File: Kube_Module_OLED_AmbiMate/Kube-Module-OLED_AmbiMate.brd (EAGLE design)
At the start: 42.8 x 54.6 mm, 9 parts

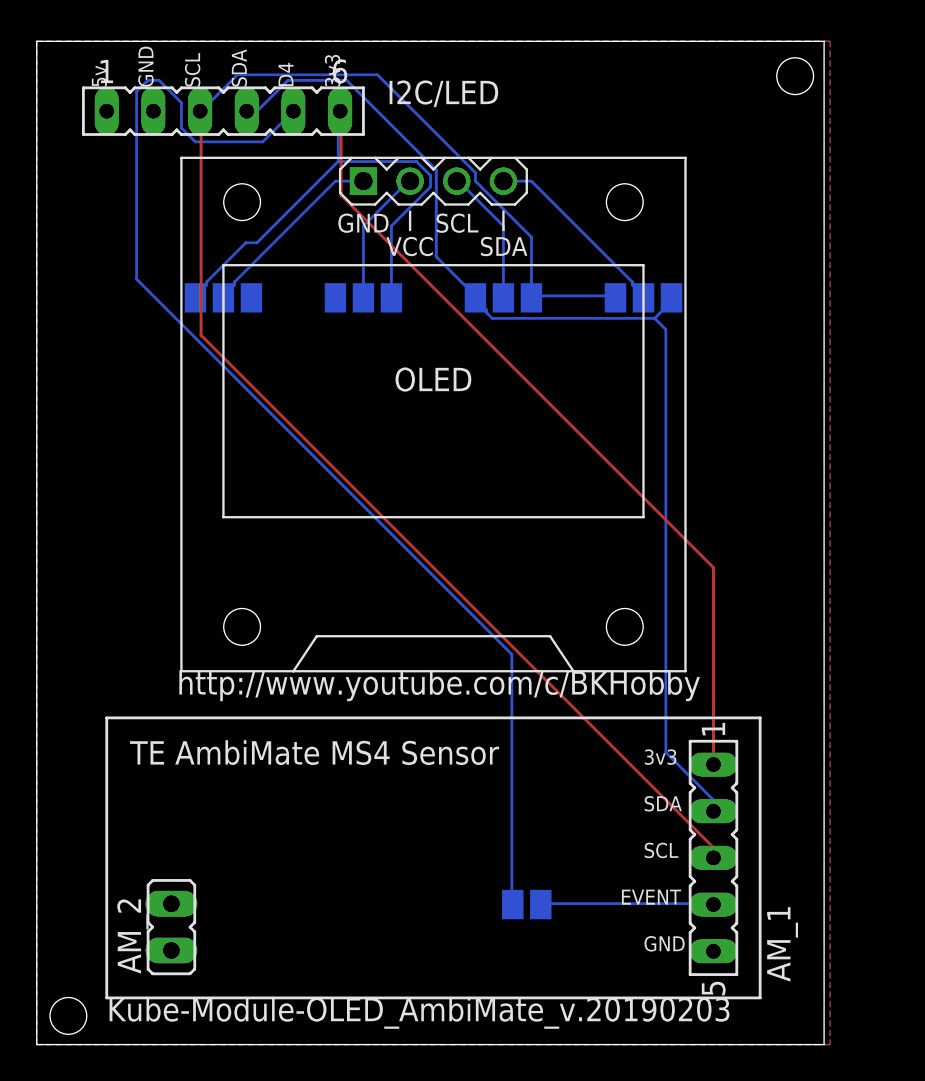
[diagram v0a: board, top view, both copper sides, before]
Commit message: Mods to OLED board to get rid of EVENT_OUT (causes boot issues since D4 needs to be held HI)
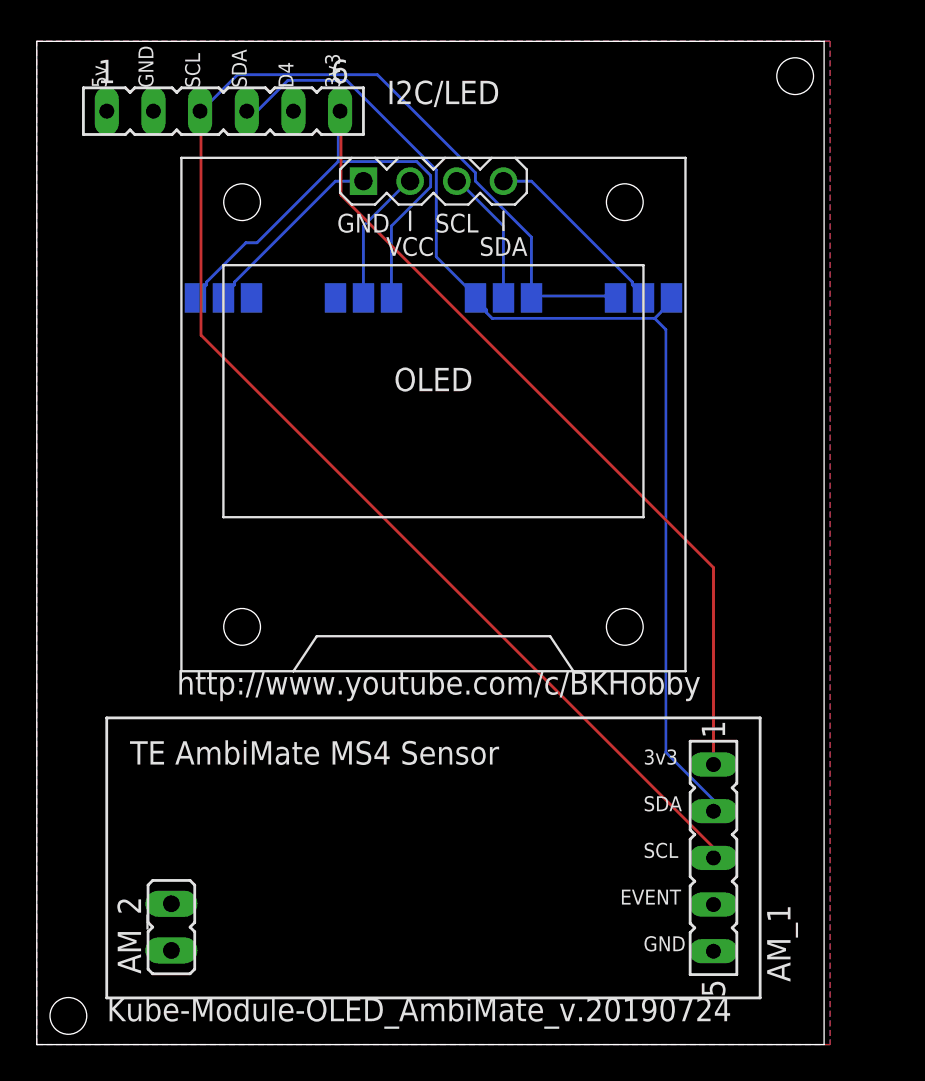
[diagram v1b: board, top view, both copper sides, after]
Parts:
- removed EVENT_OUT: (no value), jumper:SJ
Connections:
- removed net EVENT: AM_1.4, EVENT_OUT.1
- net LED(D4): no longer EVENT_OUT.2
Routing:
- net LED(D4): track 64.4 -> 0.00 mm
- net EVENT: track 9.46 -> 0.00 mm
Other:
- board text added: "Kube-Module-OLED_AmbiMate_v.20190724"
- board text removed: "Kube-Module-OLED_AmbiMate_v.20190203"
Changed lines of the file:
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@@
 <?xml version="1.0" encoding="utf-8"?>
 <!DOCTYPE eagle SYSTEM "eagle.dtd">
-<eagle version="9.3.0">
+<eagle version="9.4.2">
 <drawing>
 <settings>
-<setting alwaysvectorfont="yes"/>
+<setting alwaysvectorfont="no"/>
 <setting verticaltext="up"/>
 </settings>
@@
 <wire x1="55.88" y1="12.7" x2="20.32" y2="12.7" width="0.1524" layer="25"/>
 <text x="21.59" y="25.4" size="1.27" layer="25">TE AmbiMate MS4 Sensor</text>
-<text x="20.32" y="11.43" size="1.27" layer="25">Kube-Module-OLED_AmbiMate_v.20190203</text>
+<text x="20.32" y="11.43" size="1.27" layer="25">Kube-Module-OLED_AmbiMate_v.20190724</text>
 <text x="49.53" y="25.4" size="0.8128" layer="25">3v3</text>
 <text x="33.02" y="62.23" size="0.8128" layer="25" rot="R90">3v3</text>
@@
 <text x="20.32" y="62.23" size="0.8128" layer="25" rot="R90">5v</text>
 <text x="30.48" y="62.23" size="0.8128" layer="25" rot="R90">D4</text>
-<text x="57.15" y="11.43" size="1.27" layer="26" rot="MR0">Kube-Module-OLED_AmbiMate_v.20190203</text>
+<text x="57.15" y="11.43" size="1.27" layer="26" rot="MR0">Kube-Module-OLED_AmbiMate_v.20190724</text>
 <text x="29.21" y="49.53" size="0.8128" layer="26" rot="MR270">GND</text>
 <text x="33.02" y="49.53" size="0.8128" layer="26" rot="MR270">GND</text>
@@
 <attribute name="VALUE" x="26.75921875" y="14.013025" size="1.27" layer="27" ratio="10" rot="R90"/>
 </element>
-<element name="EVENT_OUT" library="jumper" library_urn="urn:adsk.eagle:library:252" package="SJ" package3d_urn="urn:adsk.eagle:package:15471/1" value="" x="43.18" y="17.78" smashed="yes" rot="MR0">
-<attribute name="NAME" x="44.831" y="18.923" size="1.27" layer="26" ratio="10" rot="MR0"/>
-<attribute name="VALUE" x="42.7799" y="17.78" size="0.02" layer="28" rot="MR0"/>
-</element>
 </elements>
 <signals>
@@
 <wire x1="33.0708" y1="60.96" x2="33.02" y2="60.96" width="0.1524" layer="1"/>
 </signal>
-<signal name="EVENT">
-<contactref element="AM_1" pad="4"/>
-<contactref element="EVENT_OUT" pad="1"/>
-<wire x1="53.34" y1="17.8308" x2="44.0436" y2="17.8308" width="0.1524" layer="16"/>
-<wire x1="44.0436" y1="17.8308" x2="43.942" y2="17.78" width="0.1524" layer="16"/>
-<wire x1="53.34" y1="17.8308" x2="53.34" y2="17.78" width="0.1524" layer="16"/>
-</signal>
 <signal name="5V">
 <contactref element="I2C/LED" pad="1"/>
@@
 <signal name="LED(D4)">
 <contactref element="I2C/LED" pad="5"/>
-<contactref element="EVENT_OUT" pad="2"/>
-<wire x1="42.3672" y1="31.3944" x2="42.3672" y2="17.8308" width="0.1524" layer="16"/>
-<wire x1="21.9456" y1="51.816" x2="42.3672" y2="31.3944" width="0.1524" layer="16"/>
-<wire x1="21.9456" y1="62.0268" x2="21.9456" y2="51.816" width="0.1524" layer="16"/>
-<wire x1="22.5552" y1="62.6364" x2="21.9456" y2="62.0268" width="0.1524" layer="16"/>
-<wire x1="23.1648" y1="62.6364" x2="22.5552" y2="62.6364" width="0.1524" layer="16"/>
-<wire x1="24.384" y1="61.4172" x2="23.1648" y2="62.6364" width="0.1524" layer="16"/>
-<wire x1="24.384" y1="60.0456" x2="24.384" y2="61.4172" width="0.1524" layer="16"/>
-<wire x1="25.146" y1="59.2836" x2="24.384" y2="60.0456" width="0.1524" layer="16"/>
-<wire x1="28.8036" y1="59.2836" x2="25.146" y2="59.2836" width="0.1524" layer="16"/>
-<wire x1="30.48" y1="60.96" x2="28.8036" y2="59.2836" width="0.1524" layer="16"/>
-<wire x1="42.3672" y1="17.8308" x2="42.418" y2="17.78" width="0.1524" layer="16"/>
 </signal>
 </signals>
